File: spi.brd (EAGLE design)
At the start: 34 x 33 mm, 5 parts, among them IC2 25AA080SN, IC3 25AA080P, X1 2510-

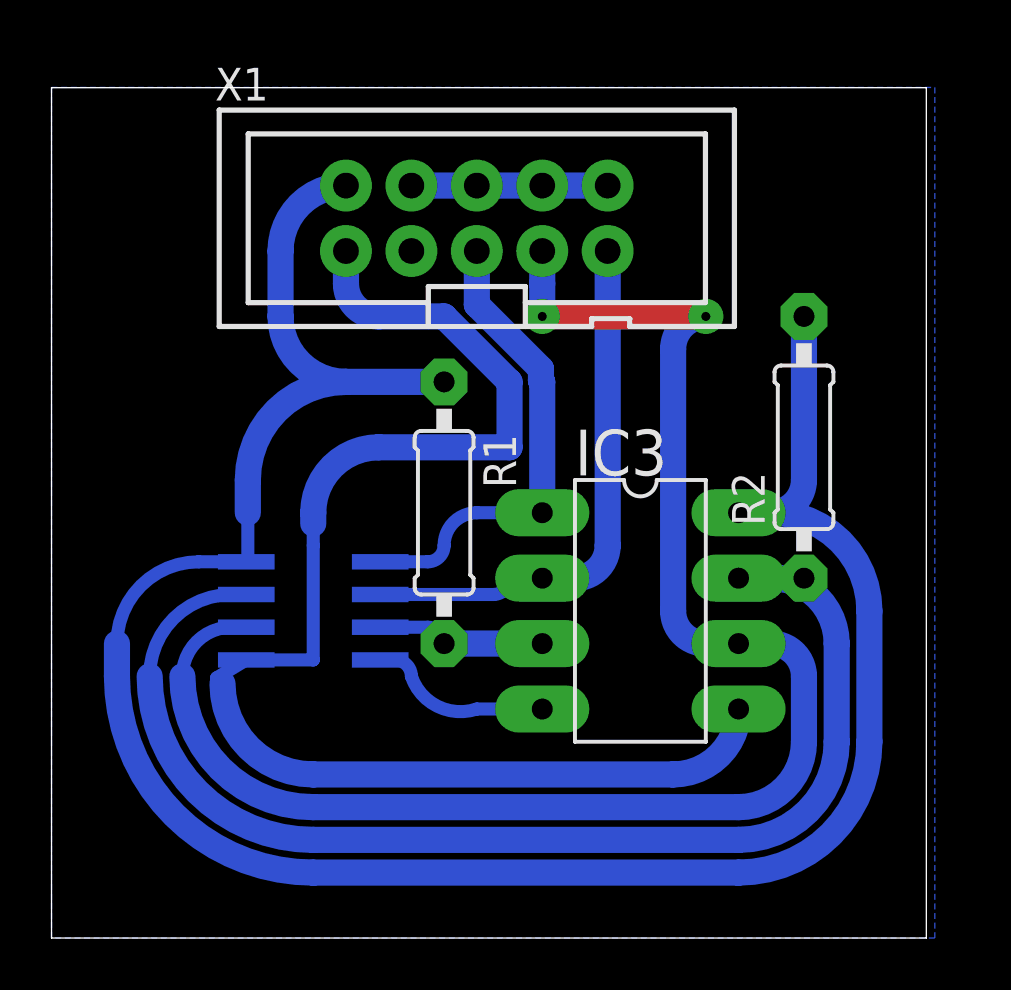
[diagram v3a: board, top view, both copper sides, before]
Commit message: Fixed spi25 label
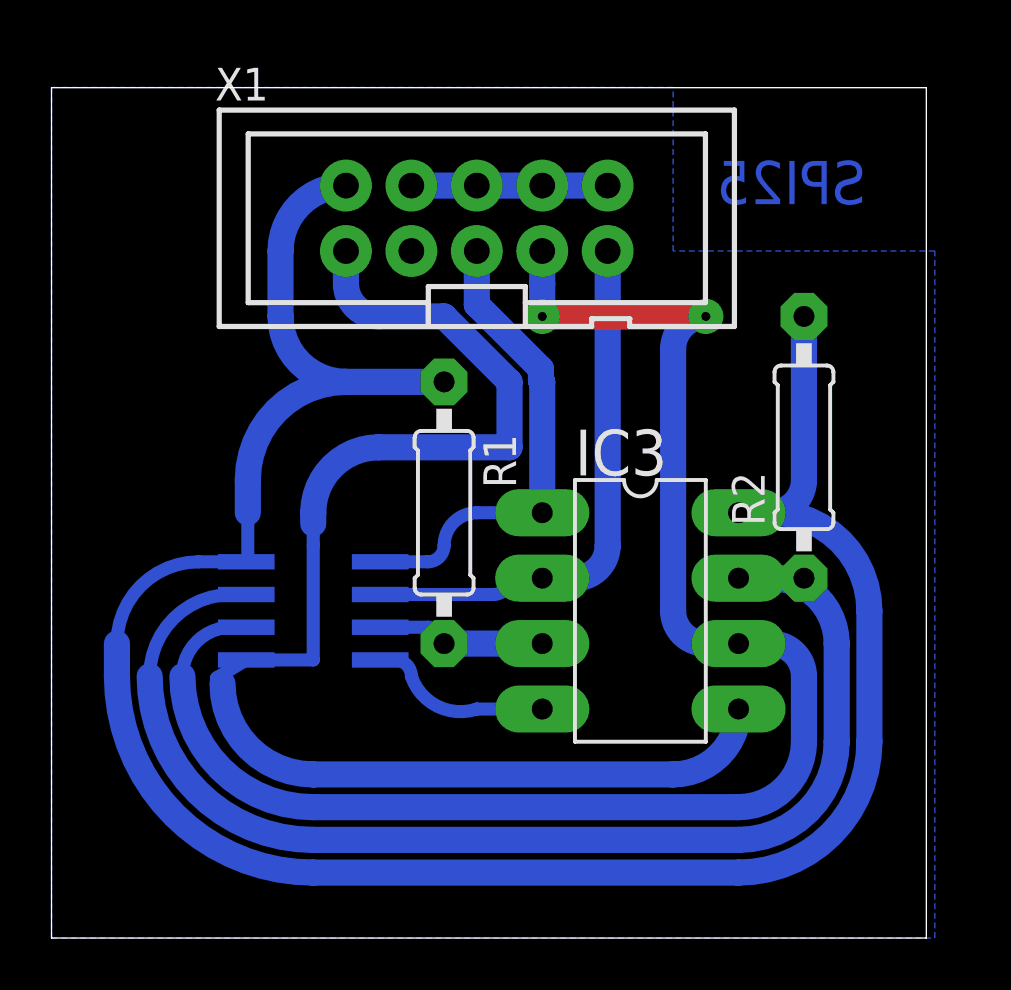
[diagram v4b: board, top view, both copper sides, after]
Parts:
- R1, R2: value (none) -> 330
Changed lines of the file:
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@@
 <grid distance="50" unitdist="mil" unit="mm" style="lines" multiple="1" display="yes" altdistance="5" altunitdist="mil" altunit="mm"/>
 <layers>
-<layer number="1" name="Top" color="4" fill="1" visible="no" active="yes"/>
+<layer number="1" name="Top" color="4" fill="1" visible="yes" active="yes"/>
 <layer number="16" name="Bottom" color="1" fill="1" visible="yes" active="yes"/>
 <layer number="17" name="Pads" color="2" fill="1" visible="yes" active="yes"/>
@@
 <vertex x="20.32" y="27.94"/>
 </polygon>
-<text x="40.64" y="45.72" size="1.778" layer="42" rot="MR0">SPI25</text>
+<text x="40.5" y="45" size="1.6764" layer="16" font="vector" ratio="9" rot="MR0">SPI25</text>
 </plain>
 <attributes>
@@
 <attribute name="OC_NEWARK" value="46F4725" x="25.4" y="44.45" size="1.778" layer="27" display="off"/>
 </element>
-<element name="R1" library="eagle-ltspice" library_urn="urn:adsk.eagle:library:217" package="0207/10" package3d_urn="urn:adsk.eagle:package:13275/1" value="" x="24.13" y="33.02" rot="R270">
+<element name="R1" library="eagle-ltspice" library_urn="urn:adsk.eagle:library:217" package="0207/10" package3d_urn="urn:adsk.eagle:package:13275/1" value="330" x="24.13" y="33.02" rot="R270">
 <attribute name="SPICEMODEL" value="NONE" x="24.13" y="33.02" size="1.778" layer="27" rot="R270" display="off"/>
 <attribute name="SPICEPREFIX" value="R" x="24.13" y="33.02" size="1.778" layer="27" rot="R270" display="off"/>
 </element>
-<element name="R2" library="eagle-ltspice" library_urn="urn:adsk.eagle:library:217" package="0207/10" package3d_urn="urn:adsk.eagle:package:13275/1" value="" x="38.1" y="35.56" rot="R90">
+<element name="R2" library="eagle-ltspice" library_urn="urn:adsk.eagle:library:217" package="0207/10" package3d_urn="urn:adsk.eagle:package:13275/1" value="330" x="38.1" y="35.56" rot="R90">
 <attribute name="SPICEMODEL" value="NONE" x="38.1" y="35.56" size="1.778" layer="27" rot="R90" display="off"/>
 <attribute name="SPICEPREFIX" value="R" x="38.1" y="35.56" size="1.778" layer="27" rot="R90" display="off"/>
@@
 <polygon width="0.3048" layer="16" isolate="0.3048">
 <vertex x="8.89" y="49.53"/>
-<vertex x="43.18" y="49.53"/>
+<vertex x="8.89" y="16.51"/>
 <vertex x="43.18" y="16.51"/>
-<vertex x="8.89" y="16.51"/>
+<vertex x="43.18" y="43.18"/>
+<vertex x="33.02" y="43.18"/>
+<vertex x="33.02" y="49.53"/>
 </polygon>
 </signal>

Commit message: Fixed polygon
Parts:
- R1, R2: value 330 -> (none); device eagle-ltspice:0207/10 -> eagle-ltspice:0204/7
- moved R2 1.80 mm to (39.4, 34.3)
- moved R1 1.27 mm to (24.1, 31.8)
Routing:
- net SI: track 52.9 -> 51.4 mm
- net HOLD: track 47.2 -> 46.1 mm
- net VCC: track 84.1 -> 84.8 mm
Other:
- board size 34 x 33 mm -> 35.2 x 33 mm
